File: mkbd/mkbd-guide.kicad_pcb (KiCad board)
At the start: 2 copper layers, 91 x 55 mm, 8 parts, among them SW1 RST, SW2 SW_PUSH, SW3 SW_PUSH, SW4 SW_PUSH, SW5 SW_PUSH, SW6 SW_PUSH, SW7 SW_PUSH, U1 ProMicro_r

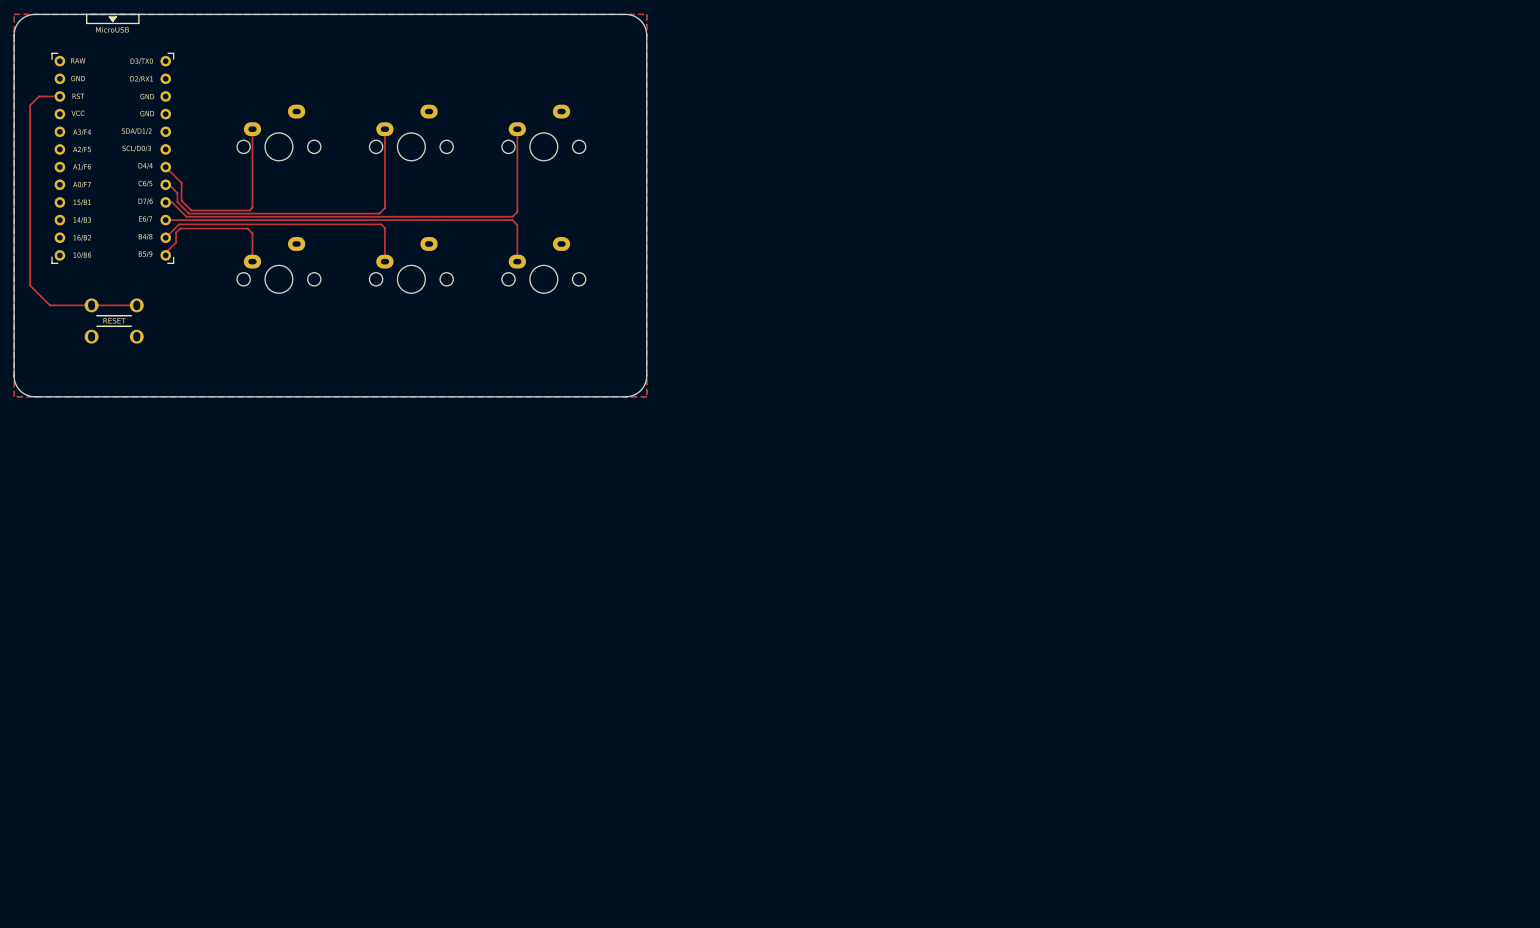
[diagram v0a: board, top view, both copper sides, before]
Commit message: Added silkscreen and gerbers
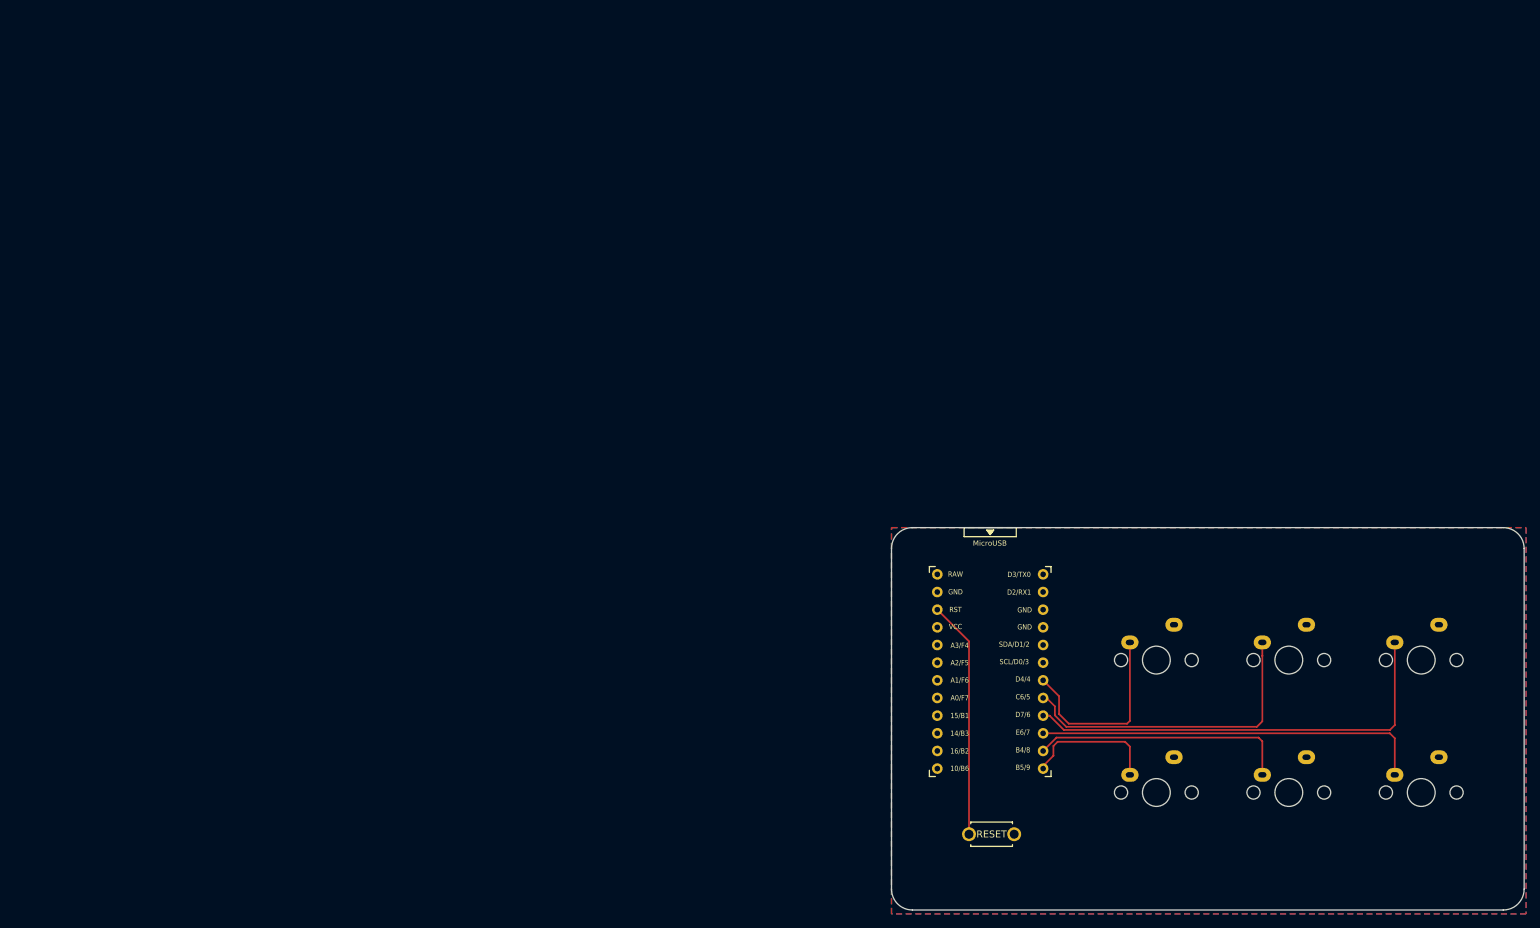
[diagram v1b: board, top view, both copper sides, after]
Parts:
- added G***: LOGO, mkbd:meishi, B.Cu at (171.8, 101.3)
- SW1: footprint kbd:ResetSW_4 -> kbd:ResetSW
- moved SW2 146.2 mm to (164.3, 92.9)
- moved SW4 146.2 mm to (202.4, 92.9)
- moved SW5 146.2 mm to (164.3, 111.9)
- moved SW7 146.2 mm to (202.4, 111.9)
- moved U1 146.2 mm to (140.4, 95.0)
- moved SW1 146.2 mm to (140.6, 117.9), turned to 0 degrees
- moved SW3 146.2 mm to (183.4, 92.9)
- moved SW6 146.2 mm to (183.4, 111.9)
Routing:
- net Net-(SW1-Pad2): track 47.3 -> 34.2 mm
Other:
- board text added: "My attempt at mkbd-guide - u/thomastrain00"
